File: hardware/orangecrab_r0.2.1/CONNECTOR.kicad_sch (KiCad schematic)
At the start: 1 part

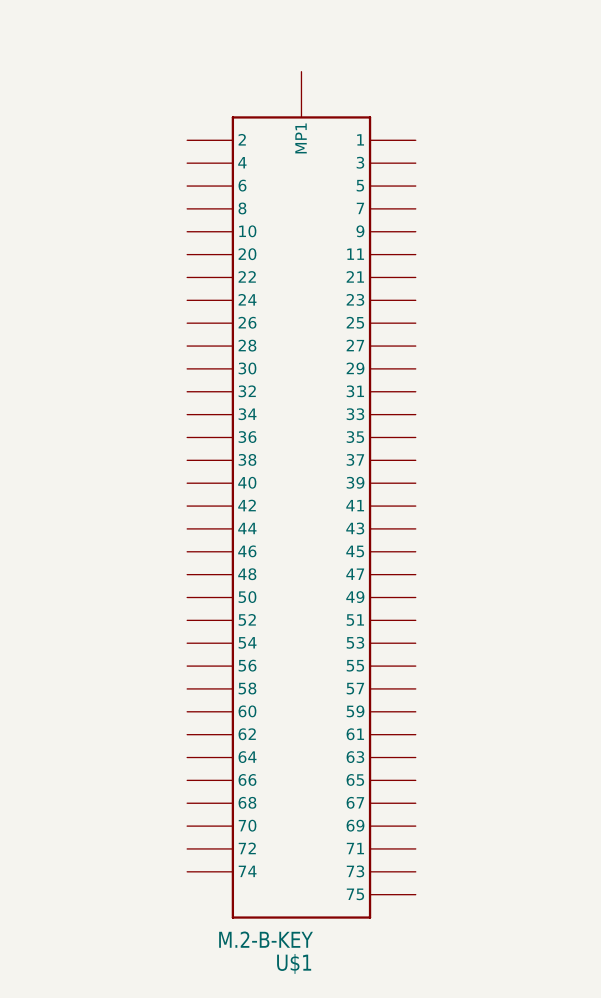
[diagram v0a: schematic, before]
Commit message: connect all spare IOs to M.2
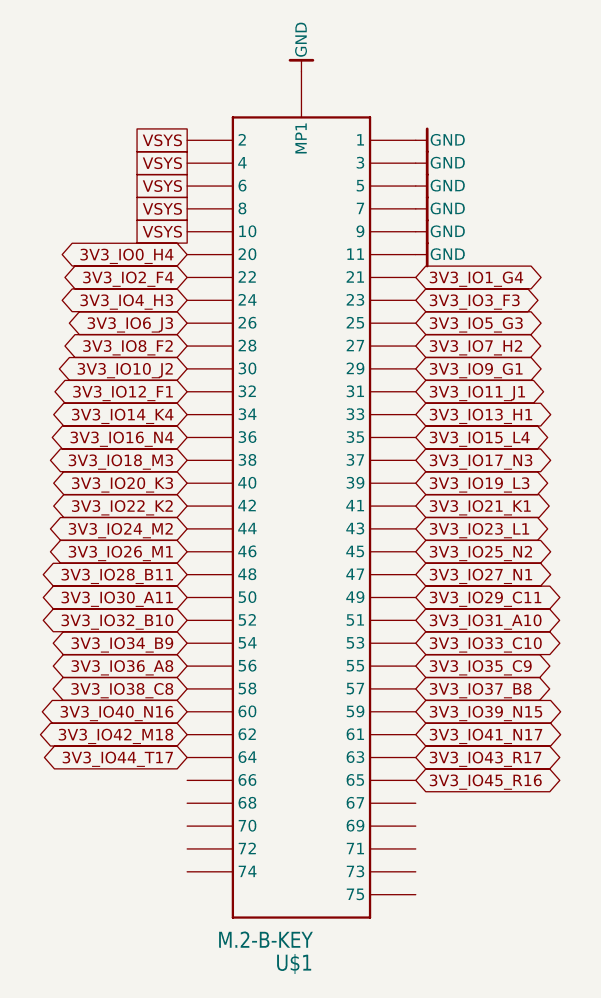
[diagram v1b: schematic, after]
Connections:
- net GND: now reaches U$1.MOUNTING-HOLE (MP1)
- net GND: now also U$1.P$1 (1), U$1.P$11 (11), U$1.P$3 (3), U$1.P$5 (5), U$1.P$7 (7), U$1.P$9 (9)
- net VSYS: now reaches U$1.P$10 (10)
- net VSYS: now also U$1.P$2 (2), U$1.P$4 (4), U$1.P$6 (6), U$1.P$8 (8)
- net 3V3_IO0_H4: now reaches U$1.P$20 (20)
- net 3V3_IO1_G4: now reaches U$1.P$21 (21)
- net 3V3_IO2_F4: now reaches U$1.P$22 (22)
- net 3V3_IO3_F3: now reaches U$1.P$23 (23)
- net 3V3_IO4_H3: now reaches U$1.P$24 (24)
- net 3V3_IO5_G3: now reaches U$1.P$25 (25)
- net 3V3_IO6_J3: now reaches U$1.P$26 (26)
- net 3V3_IO7_H2: now reaches U$1.P$27 (27)
- net 3V3_IO8_F2: now reaches U$1.P$28 (28)
- net 3V3_IO9_G1: now reaches U$1.P$29 (29)
- net 3V3_IO10_J2: now reaches U$1.P$30 (30)
- net 3V3_IO11_J1: now reaches U$1.P$31 (31)
- net 3V3_IO12_F1: now reaches U$1.P$32 (32)
- net 3V3_IO13_H1: now reaches U$1.P$33 (33)
- net 3V3_IO14_K4: now reaches U$1.P$34 (34)
- net 3V3_IO15_L4: now reaches U$1.P$35 (35)
- net 3V3_IO16_N4: now reaches U$1.P$36 (36)
- net 3V3_IO17_N3: now reaches U$1.P$37 (37)
- net 3V3_IO18_M3: now reaches U$1.P$38 (38)
- net 3V3_IO19_L3: now reaches U$1.P$39 (39)
- net 3V3_IO20_K3: now reaches U$1.P$40 (40)
- net 3V3_IO21_K1: now reaches U$1.P$41 (41)
- net 3V3_IO22_K2: now reaches U$1.P$42 (42)
- net 3V3_IO23_L1: now reaches U$1.P$43 (43)
- net 3V3_IO24_M2: now reaches U$1.P$44 (44)
- net 3V3_IO25_N2: now reaches U$1.P$45 (45)
- net 3V3_IO26_M1: now reaches U$1.P$46 (46)
- net 3V3_IO27_N1: now reaches U$1.P$47 (47)
- net 3V3_IO28_B11: now reaches U$1.P$48 (48)
- net 3V3_IO29_C11: now reaches U$1.P$49 (49)
- net 3V3_IO30_A11: now reaches U$1.P$50 (50)
- net 3V3_IO31_A10: now reaches U$1.P$51 (51)
- net 3V3_IO32_B10: now reaches U$1.P$52 (52)
- net 3V3_IO33_C10: now reaches U$1.P$53 (53)
- net 3V3_IO34_B9: now reaches U$1.P$54 (54)
- net 3V3_IO35_C9: now reaches U$1.P$55 (55)
- net 3V3_IO36_A8: now reaches U$1.P$56 (56)
- net 3V3_IO37_B8: now reaches U$1.P$57 (57)
- net 3V3_IO38_C8: now reaches U$1.P$58 (58)
- net 3V3_IO39_N15: now reaches U$1.P$59 (59)
- net 3V3_IO40_N16: now reaches U$1.P$60 (60)
- net 3V3_IO41_N17: now reaches U$1.P$61 (61)
- net 3V3_IO42_M18: now reaches U$1.P$62 (62)
- net 3V3_IO43_R17: now reaches U$1.P$63 (63)
- net 3V3_IO44_T17: now reaches U$1.P$64 (64)
- net 3V3_IO45_R16: now reaches U$1.P$65 (65)

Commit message: Clean up DRC a bit
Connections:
- net GND: no longer U$1.MOUNTING-HOLE (MP1)
- no-connect marks 0 -> 1
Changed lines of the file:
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@@
 (kicad_sch (version 20230121) (generator eeschema)
   (paper "A4")
+  (no_connect (at 152.4 43.18))
   (global_label "3V3_IO34_B9" (shape bidirectional) (at 139.7 106.68 180) (fields_autoplaced)
     (effects (font (size 1.27 1.27)) (justify right))
@@
         )
       )
-    )
-  )
-  (symbol (lib_id "gkl_power:GND") (at 152.4 43.18 180) (unit 1)
-    (in_bom yes) (on_board yes) (dnp no)
-    (property "Reference" "#PWR0146" (at 152.4 36.83 0)
-      (effects (font (size 1.27 1.27)) hide)
-    )
-    (property "Value" "GND" (at 152.4 39.624 90)
-      (effects (font (size 1.27 1.27)))
-    )
-    (property "Footprint" "" (at 154.94 34.29 0)
-      (effects (font (size 1.27 1.27)) hide)
-    )
-    (property "Datasheet" "" (at 152.4 43.18 0)
-      (effects (font (size 1.27 1.27)) hide)
-    )
-    (pin "1")
-    (instances
-      (project "OrangeCrab"
-        (path "/3fc0bb0e-dabc-4b81-bef6-ad7dd3f01477/00000000-0000-0000-0000-00005d1738db"
-          (reference "#PWR0146") (unit 1)
-        )
-        (path "/3fc0bb0e-dabc-4b81-bef6-ad7dd3f01477/79115265-87ba-4259-b432-60b778392309"
-          (reference "#PWR06") (unit 1)
-        )
-      )

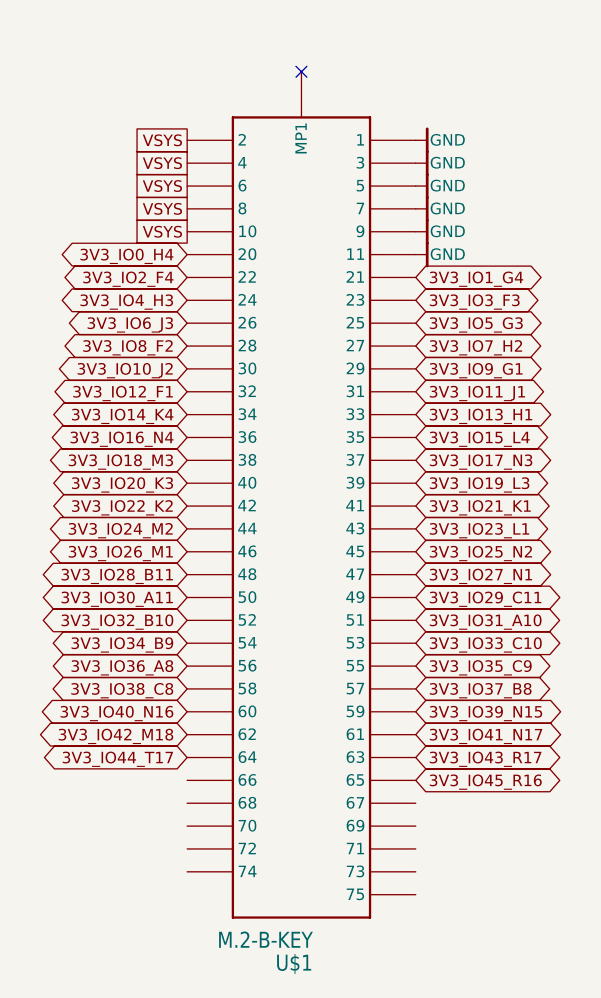
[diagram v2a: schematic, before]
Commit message: execute pinswap, not routed yet
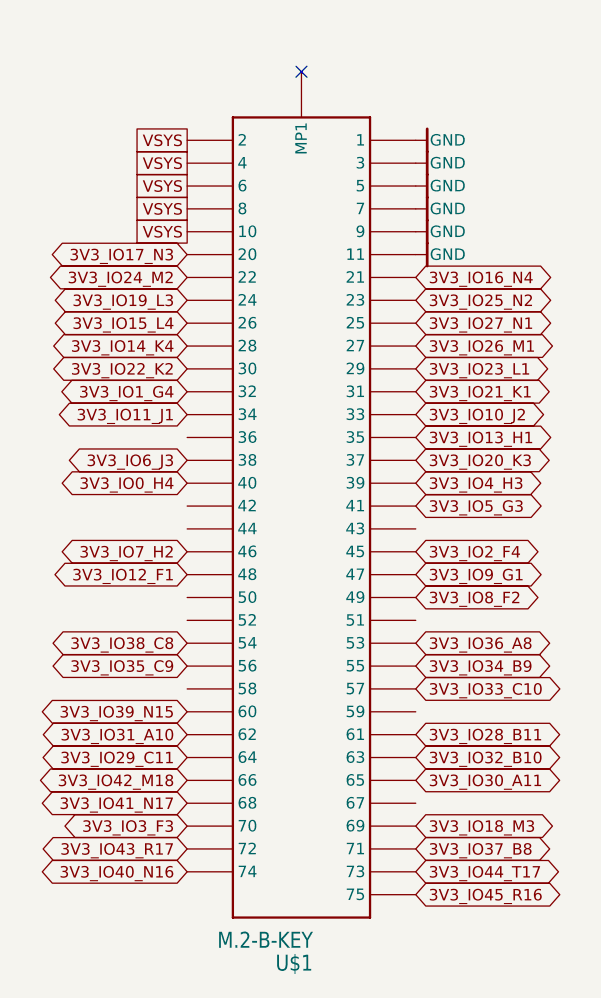
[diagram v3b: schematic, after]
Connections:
- net 3V3_IO0_H4: now also U$1.P$40 (40); no longer U$1.P$20 (20)
- net 3V3_IO10_J2: now also U$1.P$33 (33); no longer U$1.P$30 (30)
- net 3V3_IO11_J1: now also U$1.P$34 (34); no longer U$1.P$31 (31)
- net 3V3_IO12_F1: now also U$1.P$48 (48); no longer U$1.P$32 (32)
- net 3V3_IO13_H1: now also U$1.P$35 (35); no longer U$1.P$33 (33)
- net 3V3_IO14_K4: now also U$1.P$28 (28); no longer U$1.P$34 (34)
- net 3V3_IO15_L4: now also U$1.P$26 (26); no longer U$1.P$35 (35)
- net 3V3_IO16_N4: now also U$1.P$21 (21); no longer U$1.P$36 (36)
- net 3V3_IO17_N3: now also U$1.P$20 (20); no longer U$1.P$37 (37)
- net 3V3_IO18_M3: now also U$1.P$69 (69); no longer U$1.P$38 (38)
- net 3V3_IO19_L3: now also U$1.P$24 (24); no longer U$1.P$39 (39)
- net 3V3_IO1_G4: now also U$1.P$32 (32); no longer U$1.P$21 (21)
- net 3V3_IO20_K3: now also U$1.P$37 (37); no longer U$1.P$40 (40)
- net 3V3_IO21_K1: now also U$1.P$31 (31); no longer U$1.P$41 (41)
- net 3V3_IO22_K2: now also U$1.P$30 (30); no longer U$1.P$42 (42)
- net 3V3_IO23_L1: now also U$1.P$29 (29); no longer U$1.P$43 (43)
- net 3V3_IO24_M2: now also U$1.P$22 (22); no longer U$1.P$44 (44)
- net 3V3_IO25_N2: now also U$1.P$23 (23); no longer U$1.P$45 (45)
- net 3V3_IO26_M1: now also U$1.P$27 (27); no longer U$1.P$46 (46)
- net 3V3_IO27_N1: now also U$1.P$25 (25); no longer U$1.P$47 (47)
- net 3V3_IO28_B11: now also U$1.P$61 (61); no longer U$1.P$48 (48)
- net 3V3_IO29_C11: now also U$1.P$64 (64); no longer U$1.P$49 (49)
- net 3V3_IO2_F4: now also U$1.P$45 (45); no longer U$1.P$22 (22)
- net 3V3_IO30_A11: now also U$1.P$65 (65); no longer U$1.P$50 (50)
- net 3V3_IO31_A10: now also U$1.P$62 (62); no longer U$1.P$51 (51)
- net 3V3_IO32_B10: now also U$1.P$63 (63); no longer U$1.P$52 (52)
- net 3V3_IO33_C10: now also U$1.P$57 (57); no longer U$1.P$53 (53)
- net 3V3_IO34_B9: now also U$1.P$55 (55); no longer U$1.P$54 (54)
- net 3V3_IO35_C9: now also U$1.P$56 (56); no longer U$1.P$55 (55)
- net 3V3_IO36_A8: now also U$1.P$53 (53); no longer U$1.P$56 (56)
- net 3V3_IO37_B8: now also U$1.P$71 (71); no longer U$1.P$57 (57)
- net 3V3_IO38_C8: now also U$1.P$54 (54); no longer U$1.P$58 (58)
- net 3V3_IO39_N15: now also U$1.P$60 (60); no longer U$1.P$59 (59)
- net 3V3_IO3_F3: now also U$1.P$70 (70); no longer U$1.P$23 (23)
- net 3V3_IO40_N16: now also U$1.P$74 (74); no longer U$1.P$60 (60)
- net 3V3_IO41_N17: now also U$1.P$68 (68); no longer U$1.P$61 (61)
- net 3V3_IO42_M18: now also U$1.P$66 (66); no longer U$1.P$62 (62)
- net 3V3_IO43_R17: now also U$1.P$72 (72); no longer U$1.P$63 (63)
- net 3V3_IO44_T17: now also U$1.P$73 (73); no longer U$1.P$64 (64)
- net 3V3_IO45_R16: now also U$1.P$75 (75); no longer U$1.P$65 (65)
- net 3V3_IO4_H3: now also U$1.P$39 (39); no longer U$1.P$24 (24)
- net 3V3_IO5_G3: now also U$1.P$41 (41); no longer U$1.P$25 (25)
- net 3V3_IO6_J3: now also U$1.P$38 (38); no longer U$1.P$26 (26)
- net 3V3_IO7_H2: now also U$1.P$46 (46); no longer U$1.P$27 (27)
- net 3V3_IO8_F2: now also U$1.P$49 (49); no longer U$1.P$28 (28)
- net 3V3_IO9_G1: now also U$1.P$47 (47); no longer U$1.P$29 (29)

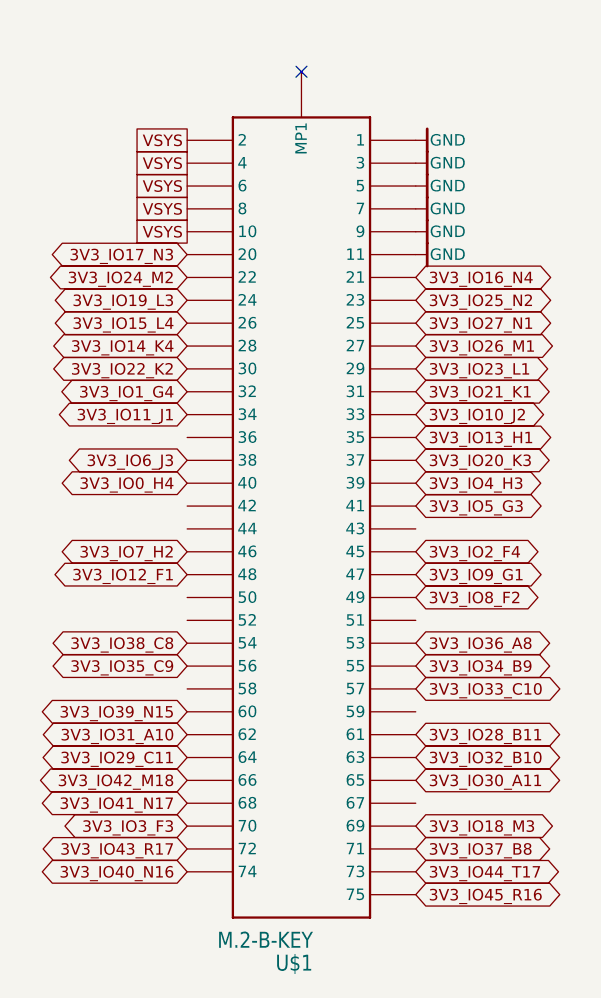
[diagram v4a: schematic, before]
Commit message: route JTAG to M.2 pads
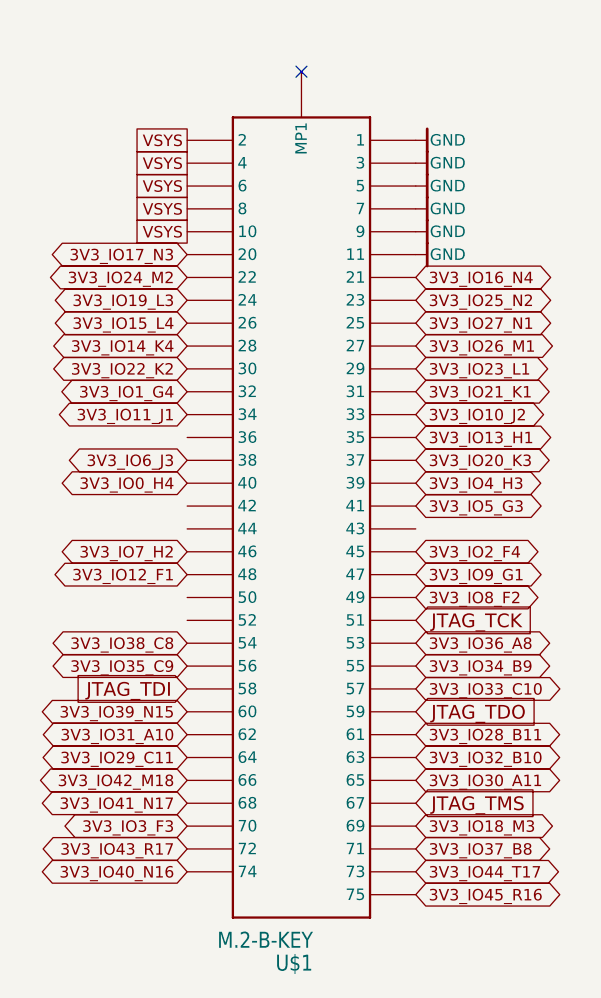
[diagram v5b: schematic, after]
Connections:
- net JTAG_TCK: now reaches U$1.P$51 (51)
- net JTAG_TDI: now reaches U$1.P$58 (58)
- net JTAG_TDO: now reaches U$1.P$59 (59)
- net JTAG_TMS: now reaches U$1.P$67 (67)
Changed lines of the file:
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@@
+    )
+  )
+  (global_label "JTAG_TMS" (shape input) (at 165.1 124.46 0)
+    (effects (font (size 1.524 1.524)) (justify left))
+    (property "Intersheetrefs" "${INTERSHEET_REFS}" (at 165.1 124.46 0)
+      (effects (font (size 1.27 1.27)) hide)
     )
   )
@@
     (property "Intersheetrefs" "${INTERSHEET_REFS}" (at 181.8696 134.62 0)
       (effects (font (size 1.27 1.27)) (justify left) hide)
+    )
+  )
+  (global_label "JTAG_TCK" (shape input) (at 165.1 104.14 0)
+    (effects (font (size 1.524 1.524)) (justify left))
+    (property "Intersheetrefs" "${INTERSHEET_REFS}" (at 165.1 104.14 0)
+      (effects (font (size 1.27 1.27)) hide)
     )
   )
@@
     )
   )
+  (global_label "JTAG_TDI" (shape input) (at 139.7 111.76 180)
+    (effects (font (size 1.524 1.524)) (justify right))
+    (property "Intersheetrefs" "${INTERSHEET_REFS}" (at 139.7 111.76 0)
+      (effects (font (size 1.27 1.27)) hide)
+    )
+  )
   (global_label "3V3_IO24_M2" (shape bidirectional) (at 139.7 66.04 180) (fields_autoplaced)
     (effects (font (size 1.27 1.27)) (justify right))
@@
     )
   )
+  (global_label "JTAG_TDO" (shape input) (at 165.1 114.3 0)
+    (effects (font (size 1.524 1.524)) (justify left))
+    (property "Intersheetrefs" "${INTERSHEET_REFS}" (at 165.1 114.3 0)
+      (effects (font (size 1.27 1.27)) hide)
+    )
+  )
